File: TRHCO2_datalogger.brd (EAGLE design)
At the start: 57.7 x 51.3 mm, 32 parts, among them J3 MicroUSB (5V), U1 ATMEGA328P-MU, U7 SHT31/35, U8 MCP1703/3.3V, Y1 16MHZ

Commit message: Minor fixes
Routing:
- net SDA: track 65.3 -> 63.5 mm
- net SCL: track 75.5 -> 75.0 mm
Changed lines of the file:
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@@
 </text>
 <text x="56.6674" y="50.419" size="0.508" layer="122" font="vector" rot="MR0">v0.1  |  January 2017</text>
-<text x="3.4036" y="50.5968" size="0.508" layer="121" font="vector" rot="R180">MISO</text>
+<text x="4.1148" y="50.6476" size="0.508" layer="121" font="vector" rot="R180">MISO</text>
 <text x="4.1148" y="48.0568" size="0.508" layer="121" font="vector" rot="R180">SCK</text>
 <text x="4.064" y="45.3644" size="0.508" layer="121" font="vector" rot="R180">RST</text>
@@
 <attribute name="PROD_ID" value="XTAL-08900" x="34.036" y="37.3126" size="1.778" layer="27" rot="R90" display="off"/>
 <attribute name="MPN" value="CSTCE16M0V53-R0" x="34.036" y="37.3126" size="1.778" layer="27" rot="R90" display="off"/>
-<attribute name="VALUE" x="36.1315" y="36.1569" size="0.508" layer="121" font="vector" rot="R90"/>
+<attribute name="VALUE" x="35.2171" y="40.2463" size="0.508" layer="121" font="vector" rot="R180"/>
 </element>
 <element name="LED1" library="adafruit" package="CHIPLED_0805" value="Status LED" x="39.4462" y="52.5272" smashed="yes" rot="R270">
@@
 <element name="C1" library="SparkFun-Capacitors" package="0805" value="1uF" x="18.3134" y="42.4688" smashed="yes">
 <attribute name="MPN" value="CC0805KKX7R7BB105" x="18.3134" y="42.4688" size="1.778" layer="27" display="off"/>
-<attribute name="VALUE" x="17.7038" y="43.561" size="0.508" layer="121" font="vector"/>
+<attribute name="VALUE" x="17.8054" y="43.561" size="0.508" layer="121" font="vector"/>
 </element>
 <element name="C6" library="SparkFun-Capacitors" package="0805" value="1uF" x="22.6822" y="40.3606" smashed="yes">
 <attribute name="MPN" value="CC0805KKX7R7BB105" x="22.6822" y="40.3606" size="1.778" layer="27" display="off"/>
-<attribute name="VALUE" x="22.0726" y="38.608" size="0.508" layer="121" font="vector"/>
+<attribute name="VALUE" x="22.0726" y="38.7096" size="0.508" layer="121" font="vector"/>
 </element>
 <element name="R13" library="SparkFun-Passives" package="0805" value="10K" x="34.925" y="29.845" smashed="yes">
@@
 <element name="C11" library="SparkFun-Capacitors" package="0805" value="0.1uF" x="23.6728" y="50.4444" smashed="yes">
 <attribute name="MPN" value="AC0805KRX7R9BB104" x="23.6728" y="50.4444" size="1.778" layer="27" display="off"/>
-<attribute name="VALUE" x="25.654" y="50.2158" size="0.508" layer="121" font="vector"/>
+<attribute name="VALUE" x="22.6568" y="48.895" size="0.508" layer="121" font="vector"/>
 </element>
 <element name="C15" library="SparkFun-Passives" package="0805" value="0.1uF" x="24.4348" y="35.2044" smashed="yes" rot="R270">
@@
 <attribute name="MF" value="Atmel" x="28.6004" y="34.8488" size="1.778" layer="27" rot="R180" display="off"/>
 <attribute name="MP" value="ATMEGA328P-MU" x="28.6004" y="34.8488" size="1.778" layer="27" rot="R180" display="off"/>
-<attribute name="VALUE" x="31.801209375" y="38.535709375" size="0.508" layer="121" font="vector" rot="R180"/>
+<attribute name="VALUE" x="31.974690625" y="37.897209375" size="0.508" layer="121" font="vector" rot="R270"/>
 </element>
 <element name="BAT1" library="SparkFun-Electromechanical" package="BATTCON_12MM" value="" x="7.1628" y="27.7368" smashed="yes" rot="R90">
@@
 <via x="26.0096" y="19.6088" extent="1-16" drill="0.254" diameter="0.127"/>
 <wire x1="26.0096" y1="19.6088" x2="26.9096" y2="20.5088" width="0.1778" layer="1" curve="90"/>
-<wire x1="40.3352" y1="6.1976" x2="41.0972" y2="5.9944" width="0.1778" layer="16"/>
-<wire x1="41.0972" y1="5.9944" x2="39.4208" y2="4.318" width="0.1778" layer="16" curve="-90"/>
 <wire x1="39.4208" y1="4.318" x2="38.1" y2="4.318" width="0.1778" layer="16"/>
 <wire x1="38.1" y1="4.318" x2="36.2204" y2="6.1976" width="0.1778" layer="16" curve="-90"/>
@@
 <wire x1="14.0716" y1="8.4836" x2="14.0716" y2="18.3388" width="0.1778" layer="16"/>
 <wire x1="14.0716" y1="18.3388" x2="15.3416" y2="19.6088" width="0.1778" layer="16" curve="-90"/>
+<wire x1="39.4208" y1="4.318" x2="41.0972" y2="5.9944" width="0.1778" layer="16" curve="90"/>
+<wire x1="41.0972" y1="5.9944" x2="41.0972" y2="6.1976" width="0.1778" layer="16"/>
 </signal>
 <signal name="SDA">
@@
 <via x="24.9936" y="20.4216" extent="1-16" drill="0.254" diameter="0.127"/>
 <wire x1="24.9936" y1="20.4216" x2="26.0096" y2="21.4376" width="0.1778" layer="1" curve="90"/>
-<wire x1="38.5572" y1="6.858" x2="37.7952" y2="6.1976" width="0.1778" layer="16"/>
 <wire x1="24.9936" y1="20.4216" x2="26.6192" y2="20.4216" width="0.1778" layer="16"/>
 <wire x1="26.6192" y1="20.4216" x2="38.608" y2="8.4328" width="0.1778" layer="16" curve="-90"/>
 <wire x1="38.608" y1="8.4328" x2="38.608" y2="6.2484" width="0.1778" layer="16"/>
-<wire x1="38.608" y1="6.2484" x2="37.7952" y2="6.1976" width="0.1778" layer="16" curve="-90"/>
+<wire x1="38.608" y1="6.2484" x2="38.5572" y2="6.1976" width="0.1778" layer="16" curve="-90"/>
 </signal>
 <signal name="N$4">
@@
 <wire x1="15.5448" y1="42.4688" x2="17.4134" y2="42.4688" width="0.4064" layer="1"/>
 <via x="13.9192" y="23.5712" extent="1-16" drill="0.254" diameter="0.127"/>
-<wire x1="26.2636" y1="23.5712" x2="42.8752" y2="6.1976" width="0.4064" layer="16" curve="-90"/>
 <contactref element="5V,500MA" pad="2"/>
-<wire x1="55.2196" y1="12.3444" x2="49.784" y2="12.3444" width="0.8128" layer="16"/>
-<wire x1="49.784" y1="12.3444" x2="42.8752" y2="6.1976" width="0.8128" layer="16" curve="90"/>
 <wire x1="17.3912" y1="39.3954" x2="17.3912" y2="27.0432" width="0.4064" layer="1"/>
 <wire x1="17.3912" y1="27.0432" x2="13.9192" y2="23.5712" width="0.4064" layer="1" curve="-90"/>
 <wire x1="26.2636" y1="23.5712" x2="13.9192" y2="23.5712" width="0.4064" layer="16"/>
+<wire x1="26.2636" y1="23.5712" x2="43.6372" y2="6.1976" width="0.4064" layer="16" curve="-90"/>
+<wire x1="43.6372" y1="6.1976" x2="49.784" y2="12.3444" width="0.8128" layer="16" curve="-90"/>
+<wire x1="49.784" y1="12.3444" x2="55.2196" y2="12.3444" width="0.8128" layer="16"/>
 </signal>
 <signal name="MISO">

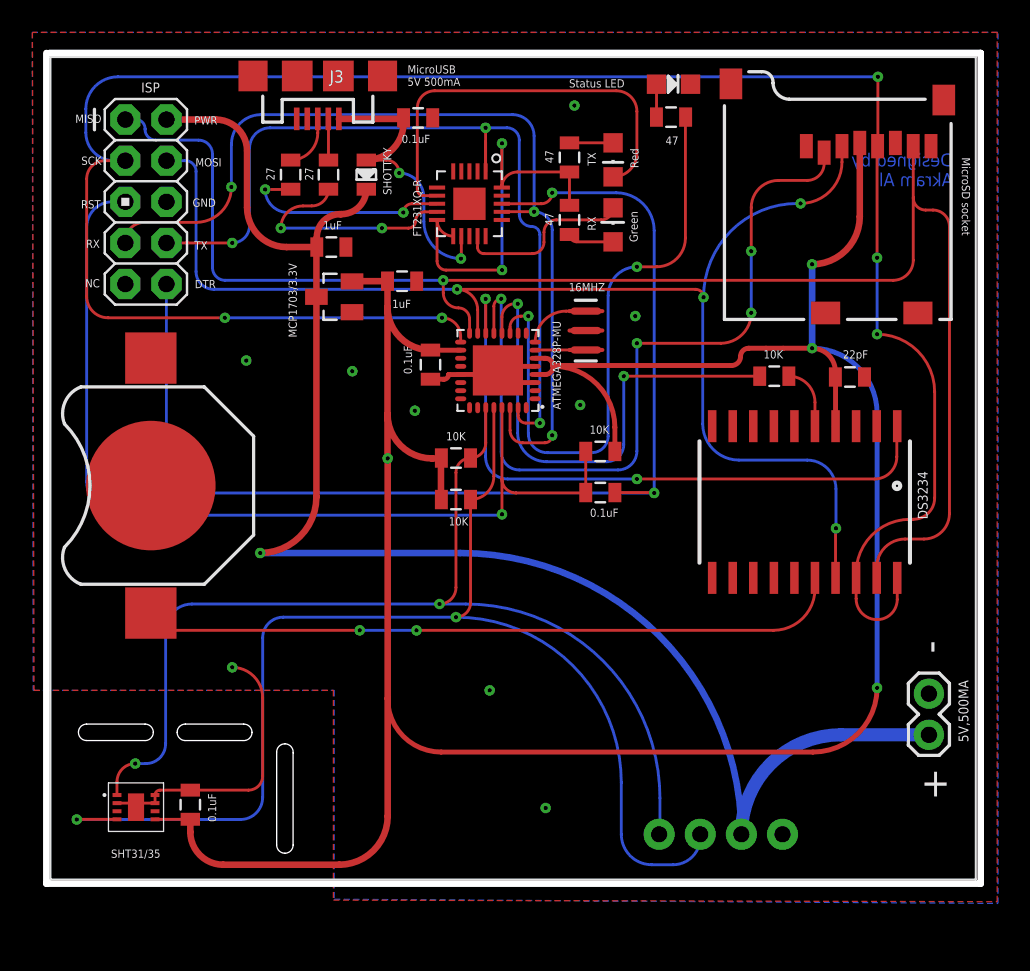
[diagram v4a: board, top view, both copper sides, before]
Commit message: v0.2 - Major fixes
- Flipped header for LiPo boost. + and - are now facing up
- Added pullup on DS3234 clock - so there is no interference while
flashing bootloader (can be removed by desoldering jumper)
- Added NPN transistor in the circuit to switch microSD card on/off for
previous adaptations of Sdfat library
- Routed CS pin of microSD card to ISP header for debug when necessary
- Added 1uF capacitor to microSD's supply
- Minor bug fixes and trace rearrangments
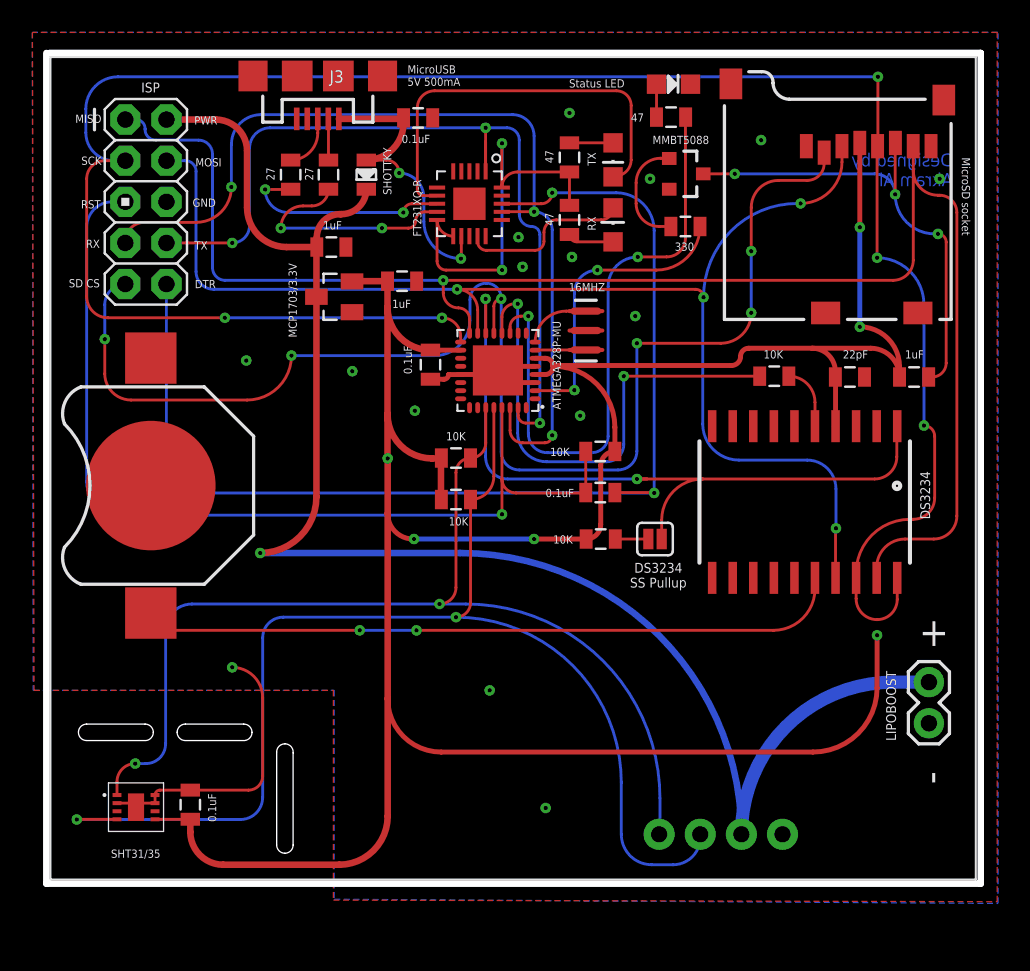
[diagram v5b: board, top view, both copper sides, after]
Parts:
- removed 5V,500MA: (no value), SparkFun-Connectors:1X02
- added C3: 1uF, SparkFun-Capacitors:0805
- added JP2: JUMPER-PAD-2-NC_BY_PASTEFULL-BOX-SILK, SparkFun-Passives:PAD-JUMPER-2-NC_BY_PASTE_YES_SILK_FULL_BOX
- added LIPOBOOST: (no value), SparkFun-Connectors:1X02
- added Q1: MMBT5088, SparkFun-DiscreteSemi:SOT23-3
- added R2: 10K, SparkFun-Resistors:0805
- added R3: 330, SparkFun-Passives:0805
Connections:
- new net D4: R3.2, U1.2
- new net GND0: C3.2, JP1.GND, Q1.3
- new net N$6: Q1.1, R3.1
- new net N$7: JP2.2, R2.1
- net D9: now also J2.9
- net GND: now also LIPOBOOST.1, Q1.2; no longer 5V,500MA.1, JP1.GND
- net PWR: now also LIPOBOOST.2; no longer 5V,500MA.2
- net SS: now also JP2.1
- net VCC: now also C3.1, R2.2
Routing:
- net D9: track 48.4 -> 83.8 mm, vias 4 -> 6
- net GND0: track 0.00 -> 28.8 mm, vias 0 -> 3
- net D4: track 0.00 -> 17.9 mm, vias 0 -> 2
- net VCC: track 166.3 -> 173.7 mm, vias 4 -> 6
- net N$6: track 0.00 -> 6.69 mm
- net SS: track 40.3 -> 45.7 mm
- net MISO: track 95.6 -> 97.8 mm
- net N$7: track 0.00 -> 2.04 mm
- net PWR: track 90.9 -> 92.2 mm
- net GND: vias 9 -> 15
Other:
- board text added: "DS3234 SS Pullup"
- board text added: "SD CS"
- board text added: "v0.2 | February 2017"
- board text removed: "NC"
- board text removed: "v0.1 | January 2017"

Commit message: v0.3 - major update
- Added boost converter (TPS61090)
- Added switch for battery
- Replaced ISP header with TagConnect pins
- Added pullups on all SPI devices
- Removed transistor from sensors and SD card
- Removed jumper @ DS3234 pull up
- Battery groove at edge
- Added LEDs for status indication
- Changed CO2 sensor dimensions to be exact
- Align USB port in center
- Removed PWR LED from booster circuir
- Changed some parts to 0402
- Replaced 16 MHz footprint
- Reroute all traces
- Added LiPo charger circuit (MCP73871)
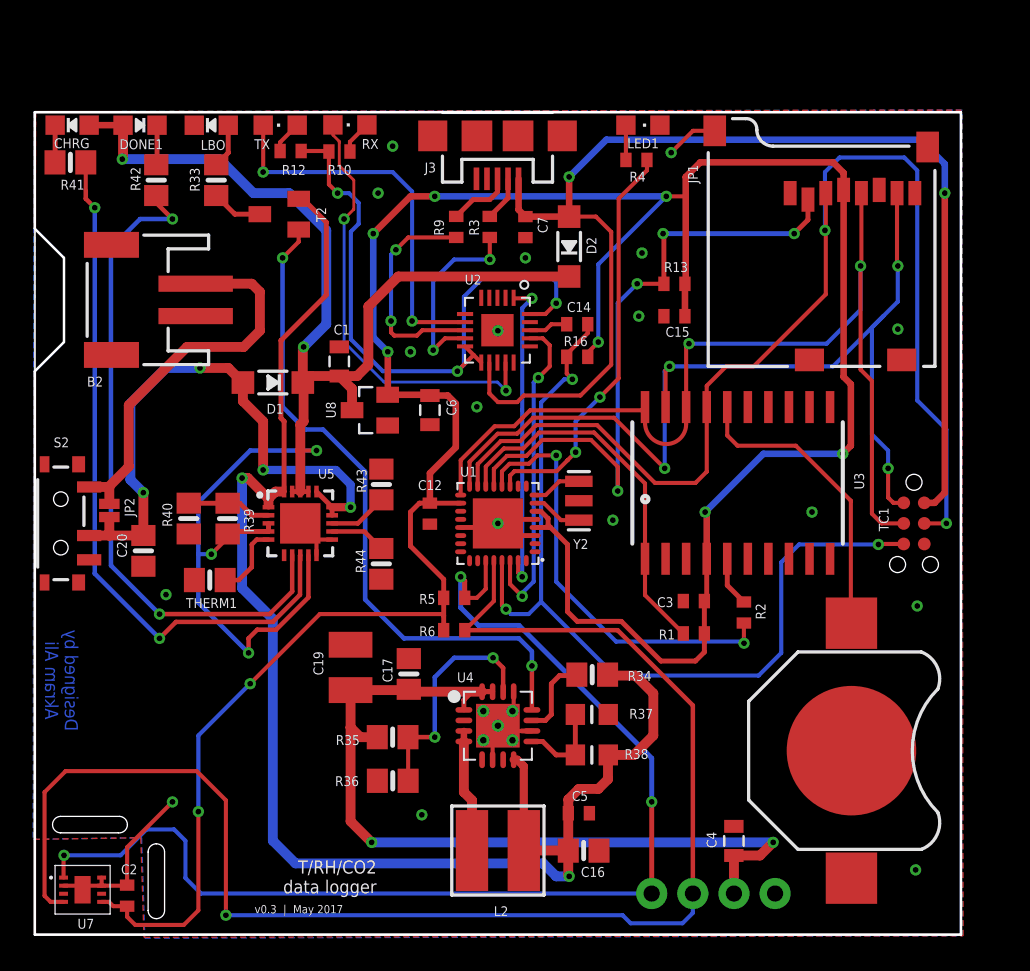
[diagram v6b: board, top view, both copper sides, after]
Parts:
- removed C11: 0.1uF, SparkFun-Capacitors:0805
- removed DS3234: DS3234, SparkFun-FreqCtrl:DS3234
- removed J2: (no value), SparkFun-Connectors:AVR_ICSP
- removed LIPOBOOST: (no value), SparkFun-Connectors:1X02
- removed Q1: MMBT5088, SparkFun-DiscreteSemi:SOT23-3
- removed R11: SHOTTKY, SparkFun-Passives:0805
- removed R21: 27, SparkFun-Passives:0805
- removed U$1: FT231XQ-R, ftdi_ft231xq-r:FTDI_FT231XQ-R_PACKAGE
- removed U$3: K30-CO2-I2C, K30-CO2-I2C:K30-CO2-I2C
- removed Y1: 16MHZ, SparkFun-FreqCtrl:RESONATOR-SMD
- added B2: JST 2-PH, microbuilder:JSTPH2
- added C14, C5, C7: 0.1uF, adafruit:C0402
- added C16, C20: 10uF, microbuilder:0805-NO
- added C17: 2.2uF, microbuilder:0805-NO
- added C19: 100uF, rcl:C1210
- added CHRG: ORANGE, microbuilder:CHIPLED_0805_NOOUTLINE
- added D1, D2: (no value), Adafruit Feather 32u4 Bluefruit LE:MICROBUILDER_SOD-123
- added DONE1: GREEN, microbuilder:CHIPLED_0805_NOOUTLINE
- added L2: 6.8uH, microbuilder:INDUCTOR_5X5MM_TDK_VLC5045
- added LBO: RED, microbuilder:CHIPLED_0805_NOOUTLINE
- added R16: 10K, adafruit:R0402
- added R33, R41, R42: 1K, microbuilder:0805-NO
- added R34, R36: 200K, microbuilder:0805-NO
- added R35: 1.87M, microbuilder:0805-NO
- added R37: 340K, microbuilder:_0805MP
- added R38: 1.87M, microbuilder:_0805MP
- added R39: 270K, microbuilder:0805-NO
- added R40, R44: 100K, microbuilder:0805-NO
- added R43: 1.0K, microbuilder:0805-NO
- added S2: (no value), SparkFun-Switches:SWITCH_SPST_SMD_A
- added T2: MMUN2133LT1G, transistor:SC59-BEC
- added TC1: TC2030-IDC-NL, TagConnect:TC2030-IDC-NL
- added THERM1: 15K, microbuilder:0805-NO
- added U2: FT231XQ-R, ftdi_ft231xq-r:FTDI_FT231XQ-R_PACKAGE
- added U3: DS3234, SparkFun-FreqCtrl:DS3234
- added U4: TPS61090RSAR, microbuilder:PVQFN-16
- added U5: MCP73871, microbuilder:QFN20_4MM
- added U6: K30-CO2-I2C, K30-CO2-I2C:K30-CO2-I2C
- added Y2: SPARKFUN_RESONATORSMD, Adafruit Feather 32u4 Bluefruit LE:SPARKFUN_RESONATOR-SMD
- C12: device SparkFun-Passives:0805 -> adafruit:C0402
- C15: value 0.1uF -> 1uF; device SparkFun-Passives:0805 -> adafruit:C0402
- C2: value 22pF -> 0.1uF; device SparkFun-Passives:0805 -> adafruit:C0402
- C3: value 1uF -> 22pF; device SparkFun-Capacitors:0805 -> adafruit:C0402
- C4: value 0.1uF -> 1uF; device SparkFun-Passives:0805 -> SparkFun-Capacitors:0805
- JP2: value JUMPER-PAD-2-NC_BY_PASTEFULL-BOX-SILK -> JUMPER-SMT_2_NO_NO-SILK; device SparkFun-Passives:PAD-JUMPER-2-NC_BY_PASTE_YES_SILK_FULL_BOX -> SparkFun-Jumpers:SMT-JUMPER_2_NO_NO-SILK
- LED1: value Status LED -> Blue
- R1, R2, R4, R5, R6: device SparkFun-Resistors:0805 -> adafruit:R0402
- R10, R13: device SparkFun-Passives:0805 -> adafruit:R0402
- R12: value 27 -> 47; device SparkFun-Passives:0805 -> adafruit:R0402
- R3: value 330 -> 27; device SparkFun-Passives:0805 -> adafruit:R0402
- R9: value 47 -> 27; device SparkFun-Passives:0805 -> adafruit:R0402
- RX: value Green -> Yellow
- TX: value Red -> Yellow
- moved C2 54.9 mm to (5.70, 2.41), turned to 90 degrees
- moved BAT1 46.3 mm to (50.4, 11.4), turned to 270 degrees
- moved JP2 33.7 mm to (4.60, 26.2), turned to 270 degrees
- moved C4 33.6 mm to (43.2, 5.79), turned to 270 degrees
- moved TX 20.7 mm to (15.2, 50.0), turned to 90 degrees
- moved C3 19.4 mm to (40.7, 20.6), turned to 180 degrees
- moved RX 17.4 mm to (19.5, 50.0), turned to 90 degrees
- moved R1 16.6 mm to (40.7, 18.6), turned to 180 degrees
- moved C15 15.4 mm to (39.5, 38.2), turned to 180 degrees
- moved R10 14.2 mm to (18.8, 48.4), turned to 0 degrees
- moved R3 12.1 mm to (28.1, 43.7), turned to 90 degrees
- moved J3 11.7 mm to (28.6, 49.3)
- moved R13 11.3 mm to (39.5, 40.2), turned to 180 degrees
- moved C12 10.6 mm to (24.4, 26.0), turned to 270 degrees
- moved R2 9.94 mm to (43.8, 19.9), turned to 90 degrees
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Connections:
- removed net D4: R3.2, U1.2
- removed net GND0: C3.2, JP1.GND, Q1.3
- removed net PWR: C1.1, J2.2, LIPOBOOST.2, R11.1, U$3.5V, U8.3
- new net 5.0V: C17.1, C19.1, C4.2, R35.2, U4.1, U4.15, U4.16, U6.5V
- new net ENABLE: R34.2, U4.11
- new net LBO: T2.B, U4.12
- new net N$14: LBO.A, R33.1
- new net N$28: R35.1, R36.2, U4.14
- new net N$30: R33.2, T2.C
- new net N$31: R39.1, R40.1, U5.P$2
- new net N$34: R42.1, U5.P$7
- new net N$35: R41.1, U5.P$8
- new net N$36: R43.2, U5.P$13
- new net N$37: THERM1.2, U5.P$5
- new net N$38: DONE1.C, R42.2
- new net N$39: CHRG.C, R41.2
- new net N$40: R44.2, U5.P$12
- new net USB_PWR: C7.1, D2.A, J3.VBUS, TC1.2, U2.VCC
- new net VBAT: C16.1, C5.1, L2.P$1, R34.1, R38.2, T2.E, U4.8, U5.P$1, U5.P$20
- new net VLIPO: C20.1, D1.A, JP2.2, S2.2, U5.P$14, U5.P$15, U5.P$16
- new net VLIPO_SWITCH: B2.2, JP2.1, S2.3
- net D8: now also R2.1; no longer R1.1
- net D9: now also R13.2; no longer J2.9
- net DTR: now also C14.1, U2.DTR#; no longer C12.1, J2.10, U$1.DTR#
- net FTDI_VCC: now also R12.1, U2.3V3OUT, U2.RESET#, U2.VCCIO; no longer R9.1, U$1.3V3OUT, U$1.RESET#, U$1.VCCIO
- net GND: now also B2.1, C12.2, C16.2, C17.2, C19.2, C2.2, C20.2, C3.2, C4.1, C5.2, C7.2, JP1.GND, LBO.C, R36.1, R37.1, R40.2, R43.1, R44.1, TC1.6, THERM1.1, U2.GND_PIN13, U2.GND_PIN21, U2.GND_PIN3, U3.10, U3.11, U3.12, U3.13, U3.14, U3.15, U3.2, U3.7, U3.8, U3.9, U4.10, U4.13, U4.5, U4.6, U4.7, U4.P$18, U4.P$19, U4.P$20, U4.P$21, U4.P$22, U4.THERMAL, U5.P$10, U5.P$11, U5.P$21, U6.GND, Y2.2; no longer C11.2, C2.1, C4.2, DS3234.10, DS3234.11, DS3234.12, DS3234.13, DS3234.14, DS3234.15, DS3234.2, DS3234.7, DS3234.8, DS3234.9, J2.6, LIPOBOOST.1, Q1.2, U$1.GND_PIN13, U$1.GND_PIN21, U$1.GND_PIN3, U$3.GND, Y1.2
- net MISO: now also TC1.1, U3.19; no longer DS3234.19, J2.1
- net MOSI: now also TC1.4, U3.17; no longer DS3234.17, J2.4
- net N$1: now also R4.2; no longer R4.1
- net N$17: now also U2.CBUS1; no longer U$1.CBUS1
- net N$18: now also U2.CBUS2; no longer U$1.CBUS2
- net N$2: now also R2.2, U3.5; no longer DS3234.5, R1.2
- net N$25: now also R3.1, U2.USBDM; no longer R21.1, U$1.USBDM
- net N$26: now also R9.1, U2.USBDP; no longer R12.1, U$1.USBDP
- net N$27: now also R10.2; no longer R9.2
- net N$29: now also R12.2; no longer R10.2
- net N$3: now also R4.1; no longer R4.2
- net N$32: now also R3.2; no longer R21.2
- net N$33: now also R9.2; no longer R12.2
- net N$4: now also Y2.3; no longer Y1.3
- net N$5: now also Y2.1; no longer Y1.1
- net N$6: now also L2.P$2, U4.3, U4.4; no longer Q1.1, R3.1
- net N$7: now also R37.2, R38.1, U4.9; no longer JP2.2, R2.1
- net N$8: now also U3.16; no longer DS3234.16
- net RESET: now also C14.2, R16.1, TC1.5; no longer C12.2, J2.5, R13.1
- net RX: now also U2.TXD; no longer J2.7, U$1.TXD
- net SCK: now also TC1.3, U3.18, U3.20; no longer DS3234.18, DS3234.20, J2.3
- net SCL: now also U6.SCL; no longer U$3.SCL
- net SDA: now also U6.SDA; no longer U$3.SDA
- net SS: now also R1.2, U3.1; no longer DS3234.1, JP2.1
- net TX: now also U2.RXD; no longer J2.8, U$1.RXD
- net VBUS: now also C1.1, CHRG.A, D1.C, D2.C, DONE1.A, R39.2, U5.P$17, U5.P$18, U5.P$19, U5.P$3, U5.P$4, U5.P$9, U8.3; no longer C11.1, J3.VBUS, R11.2, U$1.VCC
- net VCC: now also C12.1, C2.1, R1.1, R13.1, R16.2, U3.4; no longer C2.2, C4.1, DS3234.4, R13.2, R2.2
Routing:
- net VBAT: track 0.00 -> 94.9 mm, vias 0 -> 2
- net PWR: track 92.2 -> 0.00 mm, vias 1 -> 0
- net VBUS: track 18.2 -> 94.4 mm, vias 2 -> 5
- net USB_PWR: track 0.00 -> 76.1 mm, vias 0 -> 2
- net DTR: track 71.3 -> 2.43 mm, vias 2 -> 0
- net SCK: track 129.7 -> 61.0 mm, vias 5 -> 2
- net 5.0V: track 0.00 -> 52.6 mm, vias 0 -> 2
- net N$35: track 0.00 -> 43.5 mm, vias 0 -> 2
- net D9: track 83.8 -> 40.3 mm, vias 6 -> 4
- net N$34: track 0.00 -> 41.3 mm, vias 0 -> 2
- net LBO: track 0.00 -> 41.3 mm, vias 0 -> 2
- net MISO: track 97.8 -> 60.5 mm, vias 1 -> 4
- net VLIPO: track 0.00 -> 37.3 mm, vias 0 -> 4
- net RX: track 56.1 -> 20.1 mm, vias 3 -> 2
- net TX: track 52.4 -> 19.7 mm, vias 3 -> 2
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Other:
- board size 57.7 x 51.3 mm -> 57.2 x 50.8 mm
- board text added: "T/RH/CO2 data logger"
- board text added: "v0.3 | May 2017"
- board text removed: "+"
- board text removed: "-"
- board text removed: "DS3234 SS Pullup"
- board text removed: "DTR"
- board text removed: "GND"
- board text removed: "ISP"
- board text removed: "MISO"
- board text removed: "MOSI"
- board text removed: "MicroUSB 5V 500mA"
- board text removed: "PWR"
- board text removed: "RST"
- board text removed: "RX"
- board text removed: "SCK"
- board text removed: "SD CS"
- board text removed: "T/RH/CO2 datalogger"
- board text removed: "TX"
- board text removed: "v0.2 | February 2017"
